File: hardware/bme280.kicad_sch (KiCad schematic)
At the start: 8 parts, among them U6 BME280

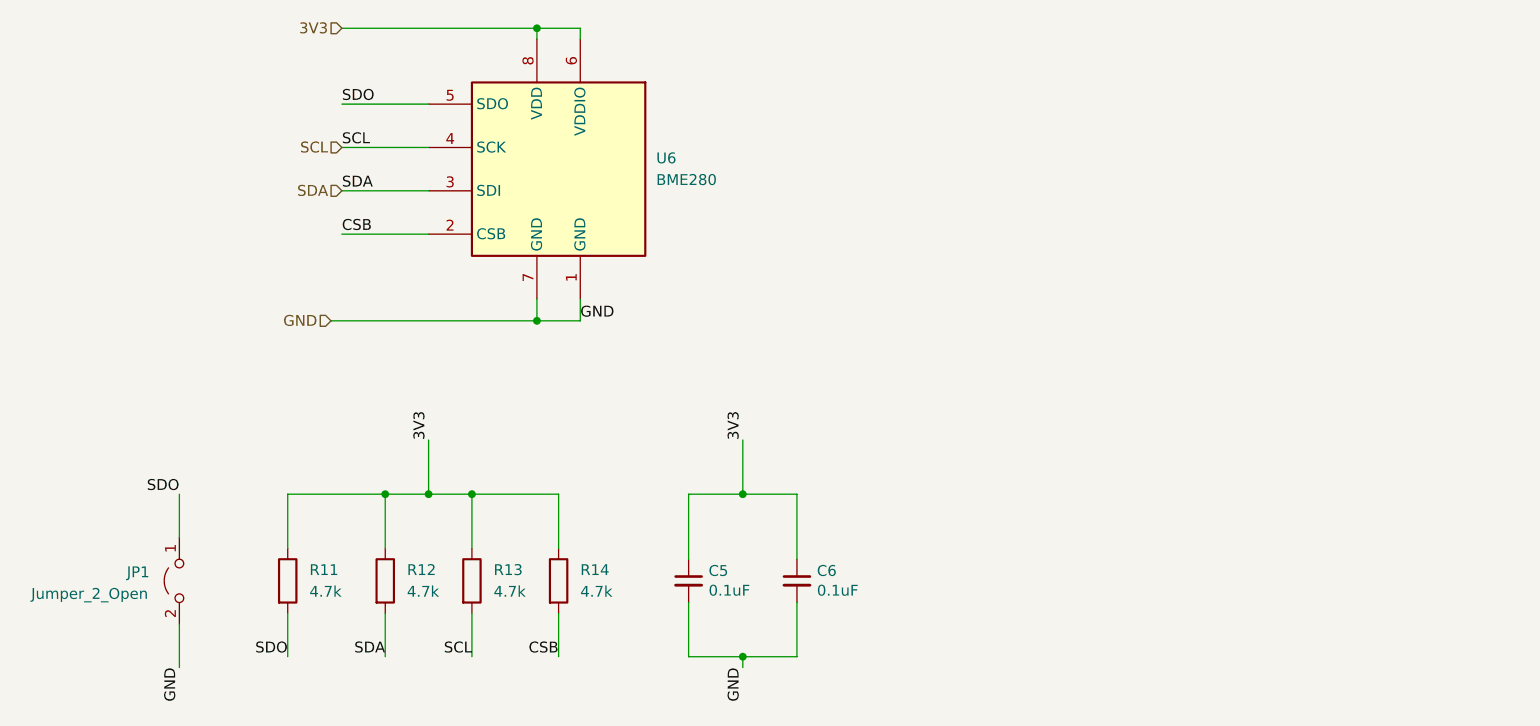
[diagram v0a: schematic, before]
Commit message: organized schem and updated readme
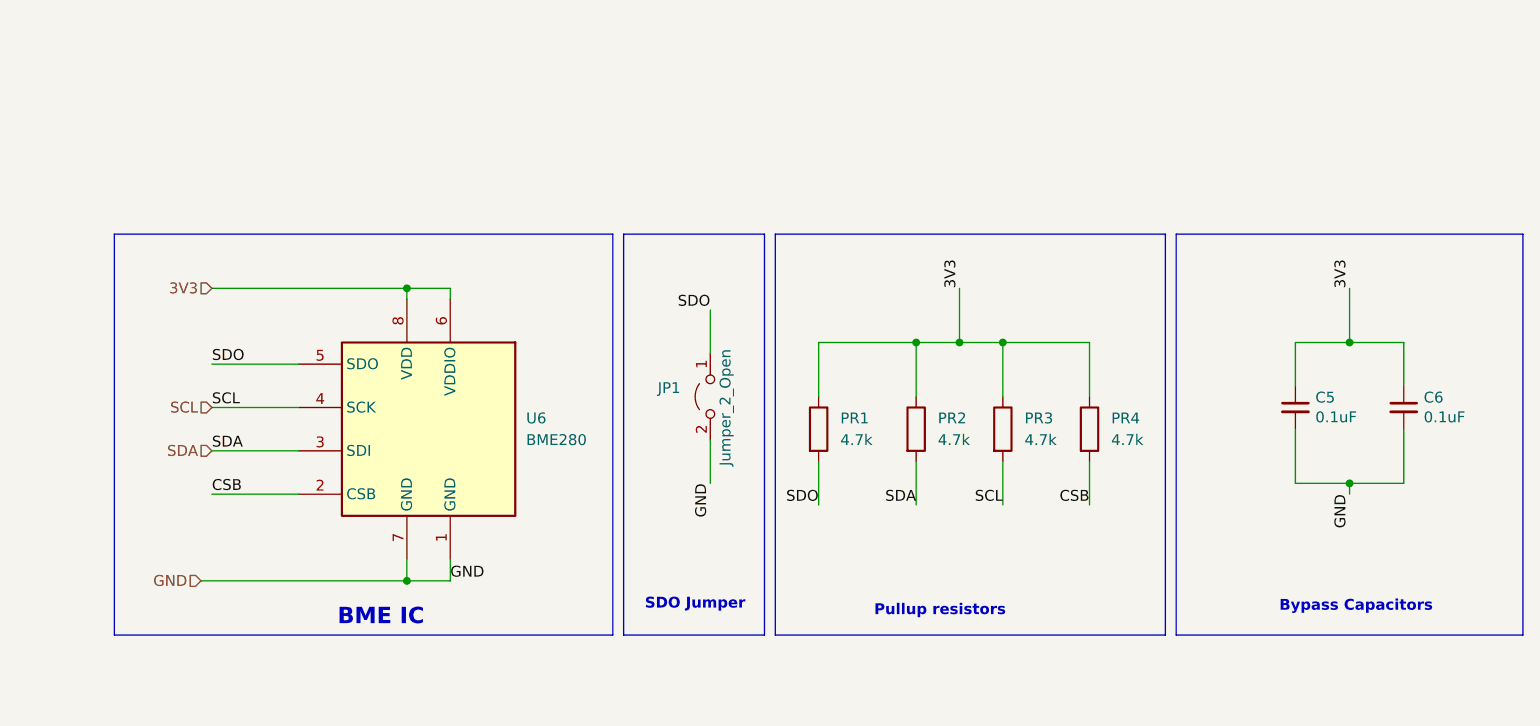
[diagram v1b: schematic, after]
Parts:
- renumbered R11 to PR1, R12 to PR2, R13 to PR3, R14 to PR4
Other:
- note added: "BME IC"
- note added: "Bypass Capacitors"
- note added: "Pullup resistors"
- note added: "SDO Jumper"
- moved on the sheet: C5, C6, JP1, PR1, PR2, PR3, PR4, U6

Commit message: completed board
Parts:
- PR1, PR2, PR3, PR4: footprint (none) -> Resistor_SMD:R_1206_3216Metric_Pad1.30x1.75mm_HandSolder
- renumbered JP1 to JP3
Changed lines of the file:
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@@
 			)
 		)
-		(property "Footprint" ""
+		(property "Footprint" "Resistor_SMD:R_1206_3216Metric_Pad1.30x1.75mm_HandSolder"
 			(at 165.862 88.9 90)
 			(effects
@@
 			)
 		)
-		(property "Footprint" ""
+		(property "Footprint" "Resistor_SMD:R_1206_3216Metric_Pad1.30x1.75mm_HandSolder"
 			(at 186.182 88.9 90)
 			(effects
@@
 			)
 		)
-		(property "Footprint" ""
+		(property "Footprint" "Resistor_SMD:R_1206_3216Metric_Pad1.30x1.75mm_HandSolder"
 			(at 154.432 88.9 90)
 			(effects
@@
 			)
 		)
-		(property "Footprint" ""
+		(property "Footprint" "Resistor_SMD:R_1206_3216Metric_Pad1.30x1.75mm_HandSolder"
 			(at 176.022 88.9 90)
 			(effects
@@
 		(on_board yes)
 		(dnp no)
-		(property "Reference" "JP1"
+		(property "Reference" "JP3"
 			(at 138.684 84.074 90)
 			(effects
@@
 			(project "BREAD_Slice"
 				(path "/66043bca-a260-4915-9fce-8a51d324c687/e7cc3cc4-19ed-4f5e-b141-abe0df9e4794"
-					(reference "JP1")
-					(unit 1)
-				)
+					(reference "JP3")
+					(unit 1)
+				)
